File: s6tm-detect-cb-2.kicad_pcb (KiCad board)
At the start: 4 copper layers, 90 x 50 mm, 173 parts, among them J1 Conn_Coaxial, J2 Conn_01x04_Pin, J3 USB_C_Receptacle_USB2.0_14P, J4 Conn_01x04, J5 Conn_01x04, J6 USB_C_Receptacle_USB2.0_14P, J7 Conn_01x04_Pin, J8 SIM_Card_Shielded, J9 Conn_Coaxial, Q1 AO3400A, Q2 MMBT3904, Q3 MMBT3904, Q4 MMBT3904, SW1 SW_Push, SW2 SW_Push, SW3 SW_Push, SW4 SW_Push, U1 W25Q128JVS, U10 TPS6282x, U11 TPS6282x, U12 TPS259472A, U13 TPD3F303DPV, U14 SIM7080G, U15 SN74LV1T125DBV, U16 SN74LV1T125DBV, U17 SN74LV1T125DBV, U18 SN74LV1T125DBV, U19 SN74LV1T125DBV, U2 SN65HVD230, U3 PCF85263ATL, U4 MS5607, U5 ESP32-S3FH4R2, U6 HTU21, U8 VL53L0CXV0DH1, U9 NextPM, Y1 32k768, Y2 48M

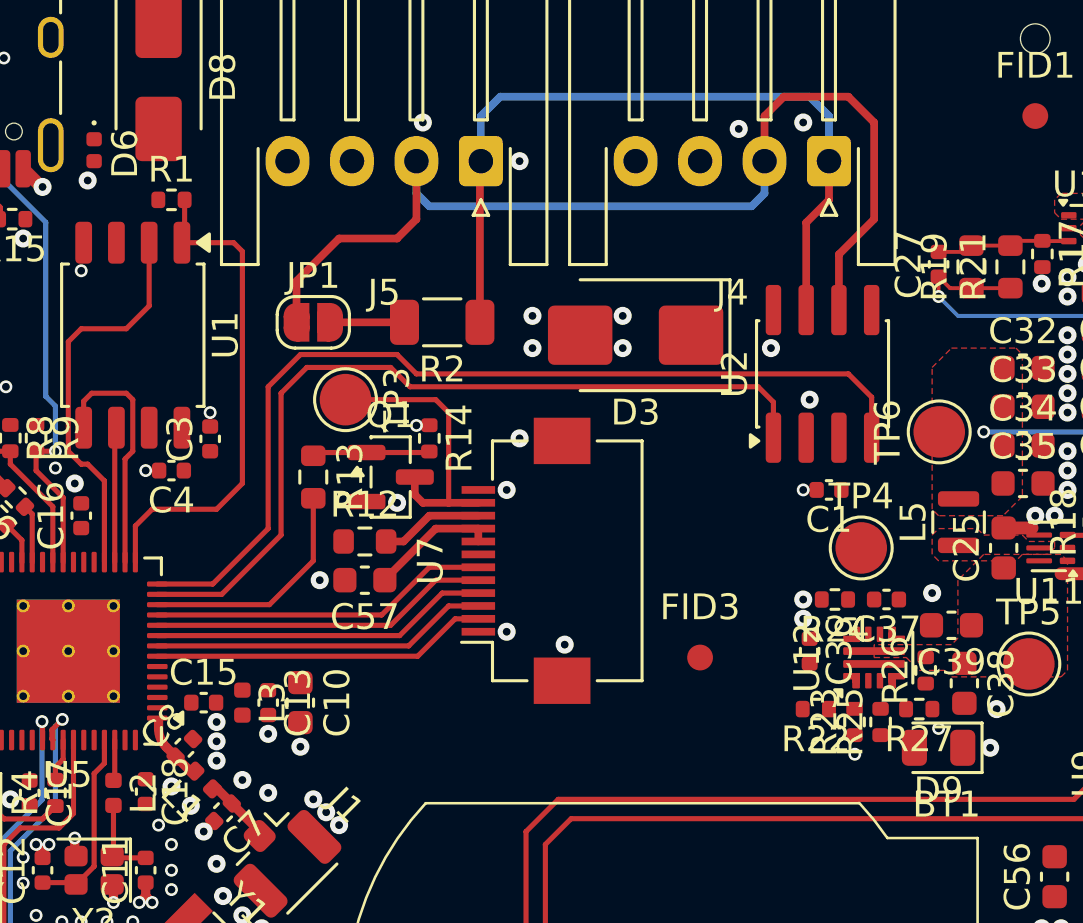
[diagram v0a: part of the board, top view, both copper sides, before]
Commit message: pcb: route efuse
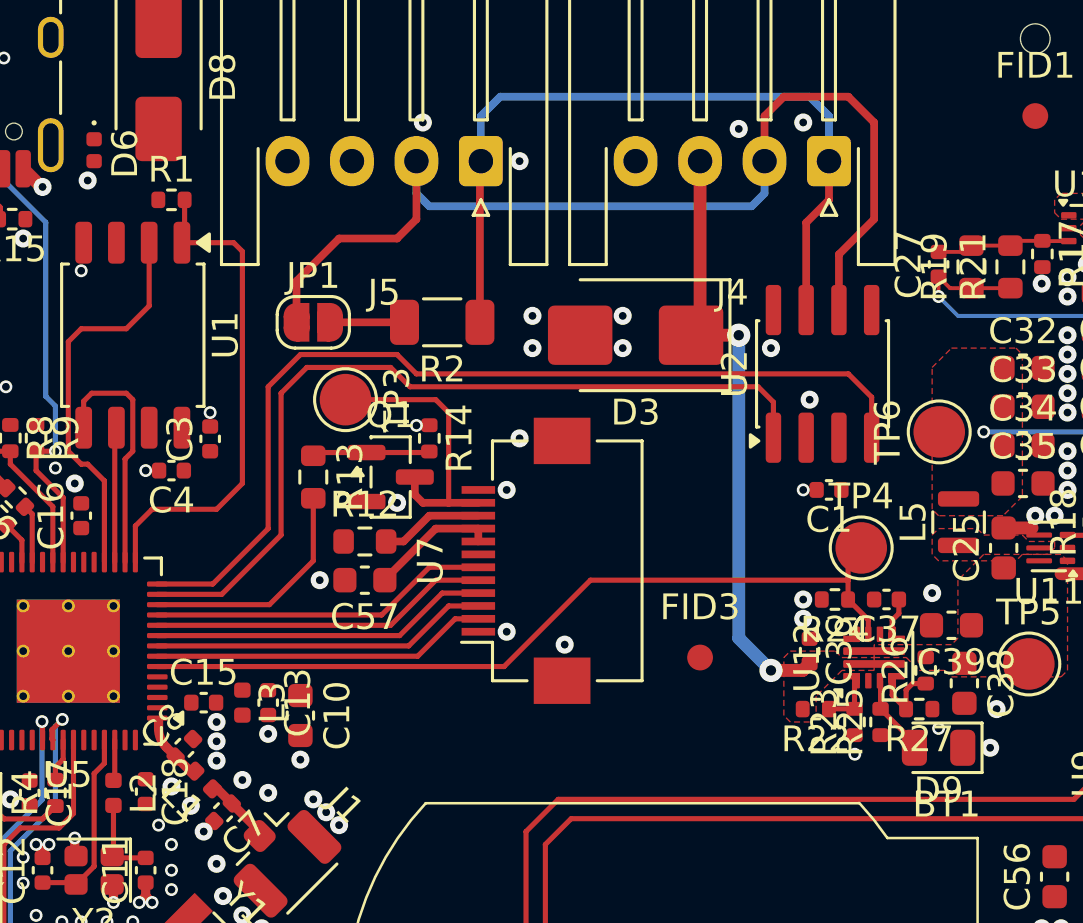
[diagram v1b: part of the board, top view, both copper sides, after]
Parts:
- moved C10 0.50 mm to (149.5, 96.2)
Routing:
- net I_EXT: track 0.00 -> 32.1 mm
- net /Power/Efuse/+VIN: track 0.00 -> 23.9 mm, vias 0 -> 2
- net Net-(D9-A): track 0.00 -> 3.15 mm
- net Net-(U12-PGTH): track 0.00 -> 2.93 mm
- net Net-(U12-EN/UVLO): track 0.00 -> 2.11 mm
- net Net-(U12-DVDT): track 0.00 -> 1.46 mm
- added copper zone on F.Cu, net /Power/Efuse/+VIN

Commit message: pcb: route pm cs
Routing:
- net /PM_CS: track 0.00 -> 87.2 mm, vias 0 -> 2
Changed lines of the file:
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@@
 	)
 	(via
-		(at 149 114.5)
+		(at 148.118875 114.055518)
 		(size 0.5)
 		(drill 0.3)
@@
 	)
 	(segment
+		(start 160.5 101)
+		(end 159.75 101.75)
+		(width 0.2)
+		(layer "F.Cu")
+		(net "/PM_CS")
+	)
+	(segment
+		(start 184.25 95.75)
+		(end 184.25 100)
+		(width 0.2)
+		(layer "F.Cu")
+		(net "/PM_CS")
+	)
+	(segment
+		(start 184 95.5)
+		(end 184.25 95.75)
+		(width 0.2)
+		(layer "F.Cu")
+		(net "/PM_CS")
+	)
+	(segment
+		(start 181.5 100.5)
+		(end 181 101)
+		(width 0.2)
+		(layer "F.Cu")
+		(net "/PM_CS")
+	)
+	(segment
+		(start 158.25 114.75)
+		(end 148.75 114.75)
+		(width 0.2)
+		(layer "F.Cu")
+		(net "/PM_CS")
+	)
+	(segment
+		(start 137.75 98.25)
+		(end 137.9 98.1)
+		(width 0.2)
+		(layer "F.Cu")
+		(net "/PM_CS")
+	)
+	(segment
+		(start 159.75 101.75)
+		(end 159.75 113.25)
+		(width 0.2)
+		(layer "F.Cu")
+		(net "/PM_CS")
+	)
+	(segment
+		(start 159.75 113.25)
+		(end 158.25 114.75)
+		(width 0.2)
+		(layer "F.Cu")
+		(net "/PM_CS")
+	)
+	(segment
+		(start 182.5 95.5)
+		(end 184 95.5)
+		(width 0.2)
+		(layer "F.Cu")
+		(net "/PM_CS")
+	)
+	(segment
+		(start 137.9 98.1)
+		(end 137.9 97.2)
+		(width 0.2)
+		(layer "F.Cu")
+		(net "/PM_CS")
+	)
+	(segment
+		(start 184.25 100)
+		(end 183.75 100.5)
+		(width 0.2)
+		(layer "F.Cu")
+		(net "/PM_CS")
+	)
+	(segment
+		(start 183.75 100.5)
+		(end 181.5 100.5)
+		(width 0.2)
+		(layer "F.Cu")
+		(net "/PM_CS")
+	)
+	(segment
+		(start 181 101)
+		(end 160.5 101)
+		(width 0.2)
+		(layer "F.Cu")
+		(net "/PM_CS")
+	)
+	(via
+		(at 137.75 98.25)
+		(size 0.5)
+		(drill 0.3)
+		(layers "F.Cu" "B.Cu")
+		(net "/PM_CS")
+	)
+	(via
+		(at 148.75 114.75)
+		(size 0.5)
+		(drill 0.3)
+		(layers "F.Cu" "B.Cu")
+		(net "/PM_CS")
+	)
+	(segment
+		(start 147.75 111)
+		(end 146.75 110)
+		(width 0.2)
+		(layer "B.Cu")
+		(net "/PM_CS")
+	)
+	(segment
+		(start 147.5 114.25)
+		(end 147.5 113.5)
+		(width 0.2)
+		(layer "B.Cu")
+		(net "/PM_CS")
+	)
+	(segment
+		(start 135.5 98.25)
+		(end 137.75 98.25)
+		(width 0.2)
+		(layer "B.Cu")
+		(net "/PM_CS")
+	)
+	(segment
+		(start 148 114.75)
+		(end 147.5 114.25)
+		(width 0.2)
+		(layer "B.Cu")
+		(net "/PM_CS")
+	)
+	(segment
+		(start 147.5 113.5)
+		(end 147.75 113.25)
+		(width 0.2)
+		(layer "B.Cu")
+		(net "/PM_CS")
+	)
+	(segment
+		(start 134.75 99)
+		(end 135.5 98.25)
+		(width 0.2)
+		(layer "B.Cu")
+		(net "/PM_CS")
+	)
+	(segment
+		(start 146.75 110)
+		(end 136.25 110)
+		(width 0.2)
+		(layer "B.Cu")
+		(net "/PM_CS")
+	)
+	(segment
+		(start 136.25 110)
+		(end 134.75 108.5)
+		(width 0.2)
+		(layer "B.Cu")
+		(net "/PM_CS")
+	)
+	(segment
+		(start 147.75 113.25)
+		(end 147.75 111)
+		(width 0.2)
+		(layer "B.Cu")
+		(net "/PM_CS")
+	)
+	(segment
+		(start 134.75 108.5)
+		(end 134.75 99)
+		(width 0.2)
+		(layer "B.Cu")
+		(net "/PM_CS")
+	)
+	(segment
+		(start 148.75 114.75)
+		(end 148 114.75)
+		(width 0.2)
+		(layer "B.Cu")
+		(net "/PM_CS")
+	)
+	(segment

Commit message: pcb: route modem
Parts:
- moved TP10 7.25 mm to (118.2, 113.8)
- moved TP12 0.50 mm to (113.5, 80.2)
- turned SW4 to 90 degrees
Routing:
- net LTE_PWR: track 0.00 -> 41.1 mm
- net Net-(U14-USB_BOOT): track 0.00 -> 22.3 mm
- net /BTN: track 0.00 -> 18.6 mm
- net Net-(Q4-C): track 0.00 -> 12.1 mm
- net /Cellular/STATUS: track 0.00 -> 6.88 mm
- net Net-(D13-K): track 0.00 -> 2.86 mm
- net /Cellular/NETLIGHT: track 0.00 -> 2.83 mm
- net Net-(Q4-B): track 0.00 -> 2.74 mm
- net Net-(Q3-B): track 0.00 -> 2.73 mm
- net Net-(Q2-B): track 0.00 -> 2.72 mm
- net Net-(D14-K): track 0.00 -> 2.56 mm
- net Net-(D13-A): track 0.00 -> 1.68 mm
- net Net-(D14-A): track 0.00 -> 1.34 mm

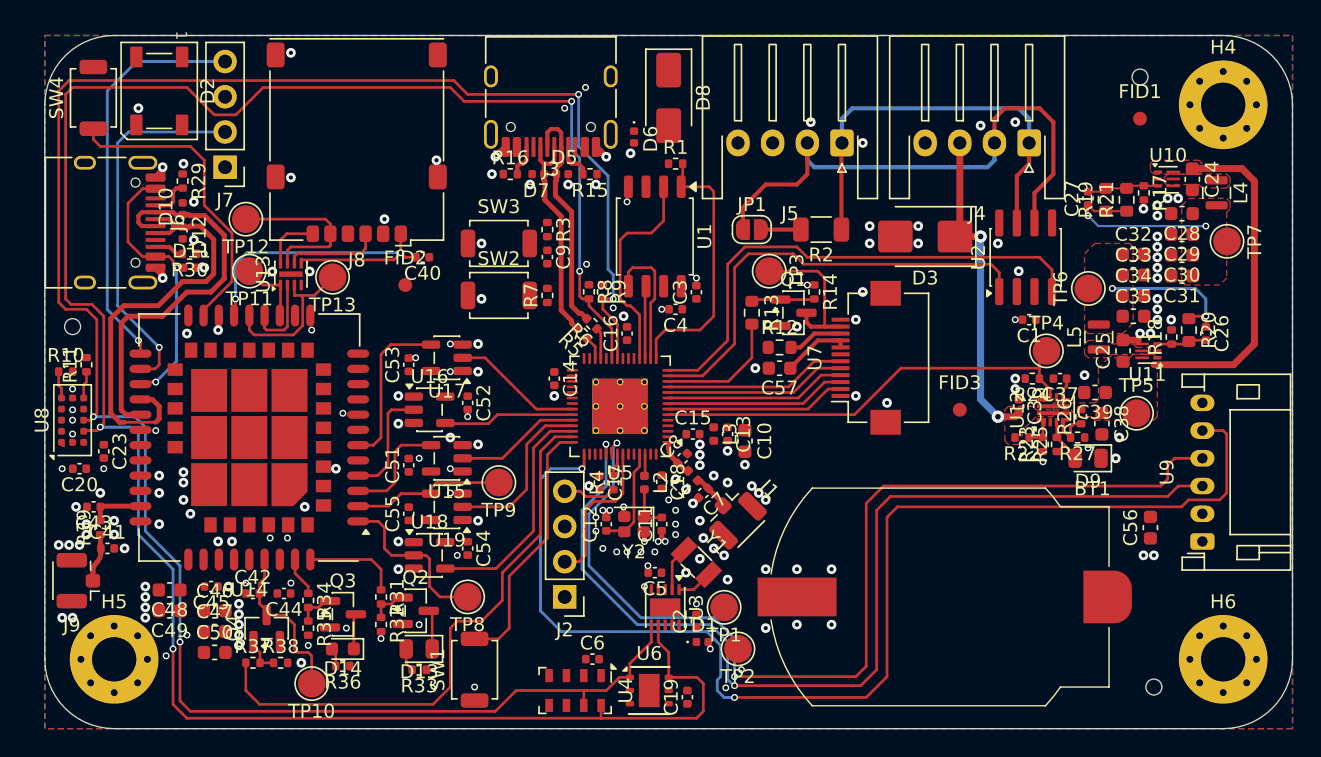
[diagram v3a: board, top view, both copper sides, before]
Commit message: pcb: route temperature sensors
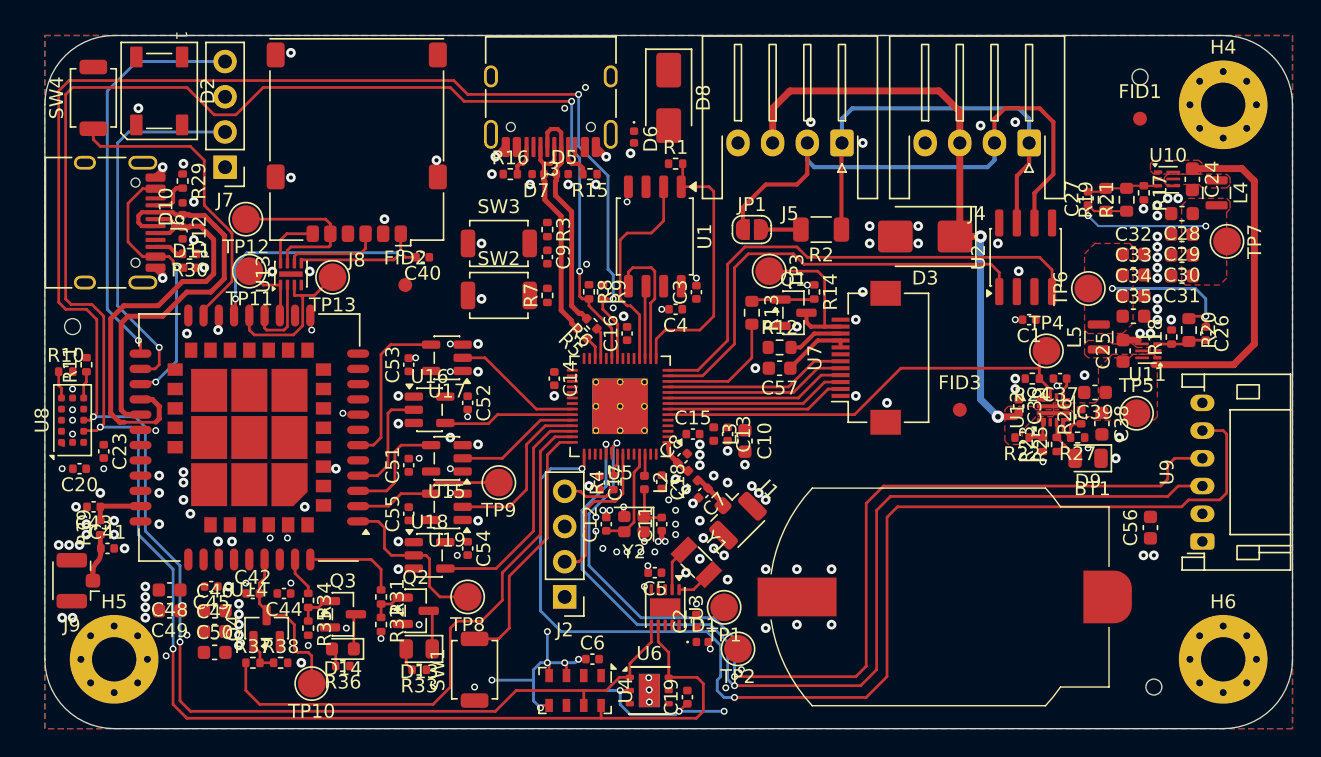
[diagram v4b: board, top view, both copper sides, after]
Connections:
- U6 pad 7: unconnected-(U6-DAP-Pad7) -> EPAD
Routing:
- net GND: track 8.76 -> 40.4 mm, vias 198 -> 208
- net /Power/Efuse/+VIN: track 23.9 -> 43.3 mm
- net EPAD: vias 0 -> 3

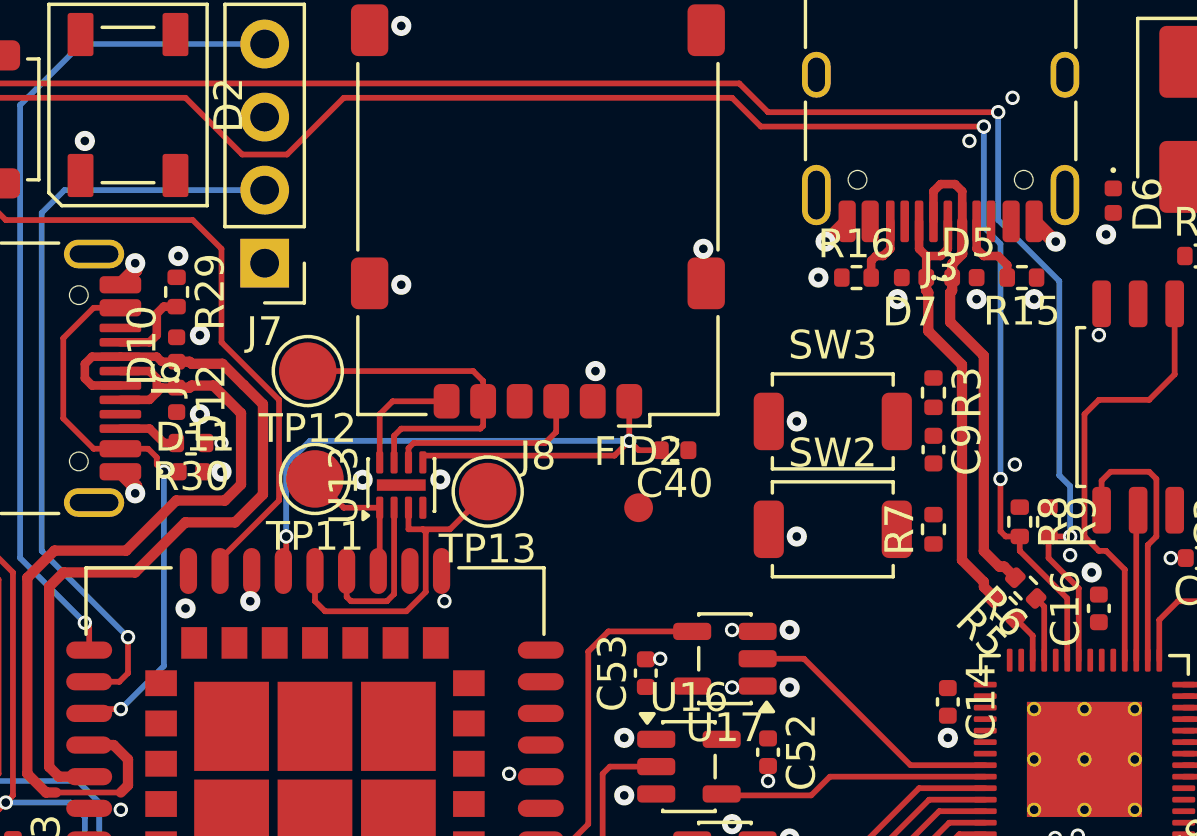
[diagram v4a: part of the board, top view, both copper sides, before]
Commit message: pcb: route rgb
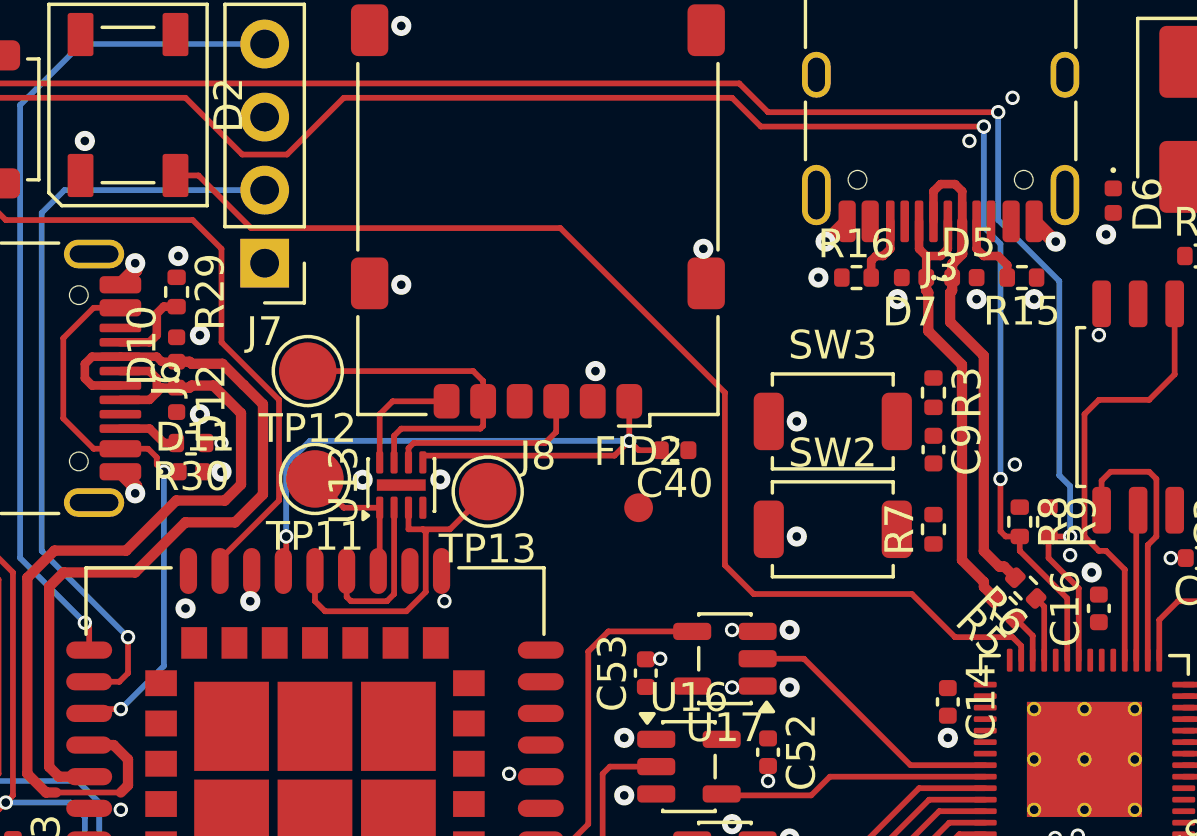
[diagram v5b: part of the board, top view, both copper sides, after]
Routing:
- net /RGB: track 0.00 -> 40.2 mm
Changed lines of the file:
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@@
+	)
+	(segment
+		(start 128 81)
+		(end 122.278843 75.278843)
+		(width 0.2)
+		(layer "F.Cu")
+		(net "/RGB")
+	)
+	(segment
+		(start 136 89.5)
+		(end 134.5 88)
+		(width 0.2)
+		(layer "F.Cu")
+		(net "/RGB")
+	)
+	(segment
+		(start 122.278843 75.278843)
+		(end 111.528843 75.278843)
+		(width 0.2)
+		(layer "F.Cu")
+		(net "/RGB")
+	)
+	(segment
+		(start 111.528843 75.278843)
+		(end 109.7 73.45)
+		(width 0.2)
+		(layer "F.Cu")
+		(net "/RGB")
+	)
+	(segment
+		(start 129 88)
+		(end 128 87)
+		(width 0.2)
+		(layer "F.Cu")
+		(net "/RGB")
+	)
+	(segment
+		(start 138.3 89.8)
+		(end 138 89.5)
+		(width 0.2)
+		(layer "F.Cu")
+		(net "/RGB")
+	)
+	(segment
+		(start 134.5 88)
+		(end 129 88)
+		(width 0.2)
+		(layer "F.Cu")
+		(net "/RGB")
+	)
+	(segment
+		(start 138.3 90.3)
+		(end 138.3 89.8)
+		(width 0.2)
+		(layer "F.Cu")
+		(net "/RGB")
+	)
+	(segment
+		(start 128 87)
+		(end 128 81)
+		(width 0.2)
+		(layer "F.Cu")
+		(net "/RGB")
+	)
+	(segment
+		(start 109.7 73.45)
+		(end 108.9 73.45)
+		(width 0.2)
+		(layer "F.Cu")
+		(net "/RGB")
+	)
+	(segment
+		(start 138 89.5)
+		(end 136 89.5)
+		(width 0.2)
+		(layer "F.Cu")
+		(net "/RGB")
 	)
 	(segment

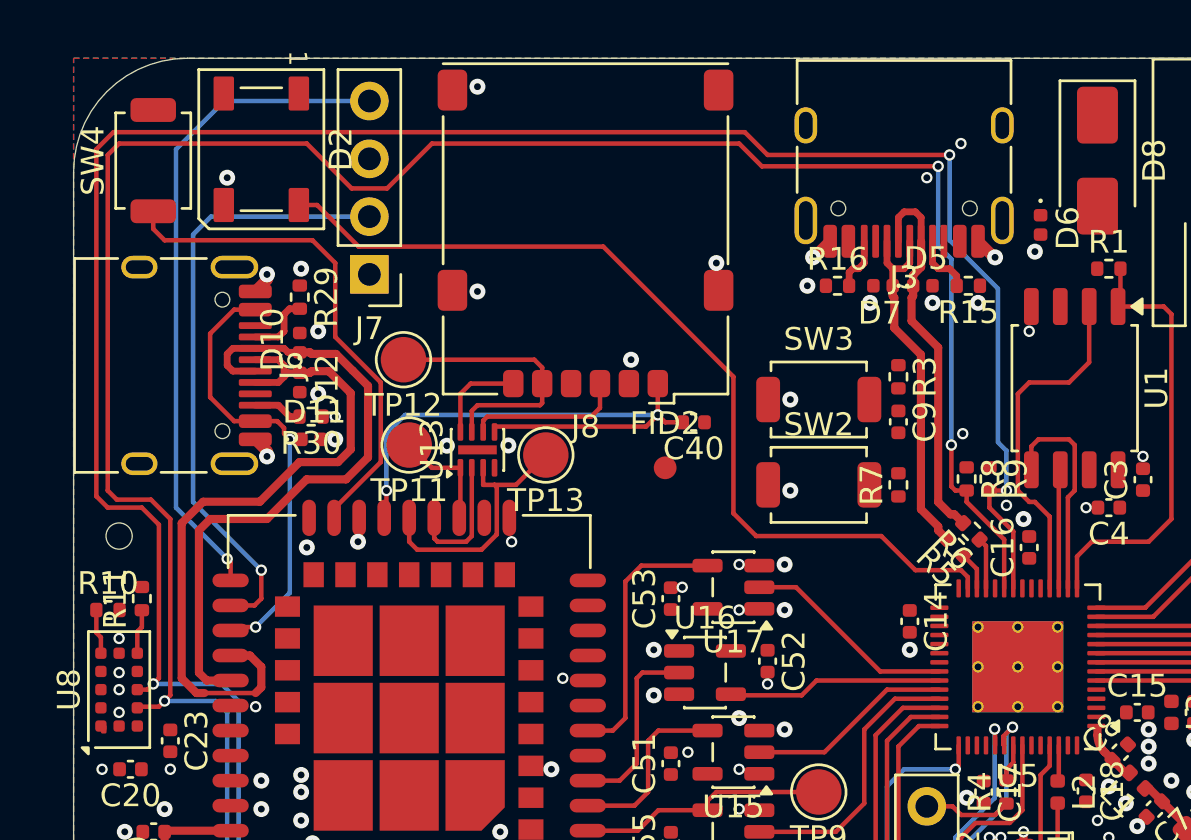
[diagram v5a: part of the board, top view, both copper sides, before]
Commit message: pcb: route tof
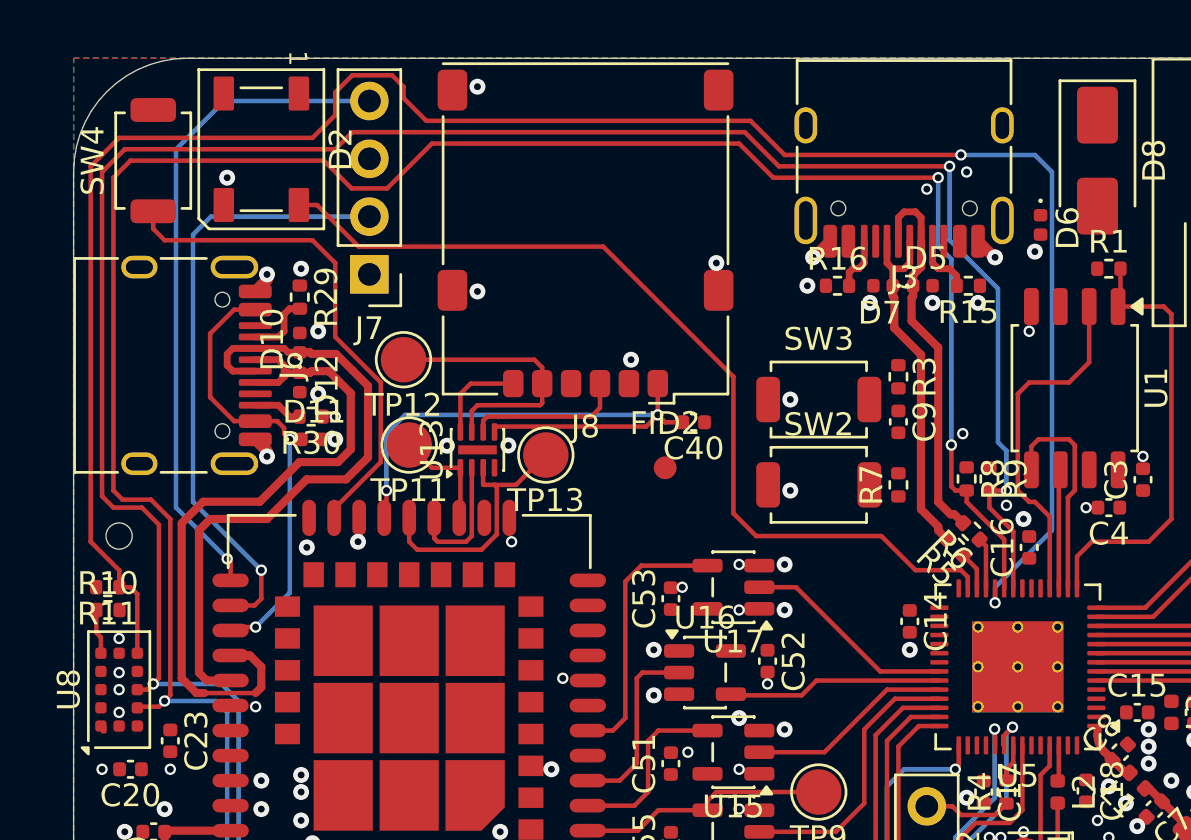
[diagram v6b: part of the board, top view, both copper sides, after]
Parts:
- moved R11 1.58 mm to (100.5, 90.2), turned to 180 degrees
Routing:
- net /TOF_INT: track 1.97 -> 89.7 mm, vias 0 -> 2
- net /SCL: track 158.3 -> 156.3 mm
- net /SDA: track 150.2 -> 148.8 mm
